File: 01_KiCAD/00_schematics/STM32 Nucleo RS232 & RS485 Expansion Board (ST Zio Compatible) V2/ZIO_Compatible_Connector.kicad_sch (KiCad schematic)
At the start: 8 parts, among them CN1 Conn_02x10_Odd_Even, CN2 Conn_02x08_Odd_Even, CN3 Conn_02x17_Odd_Even, CN4 Conn_02x15_Odd_Even, Q1 BSS84

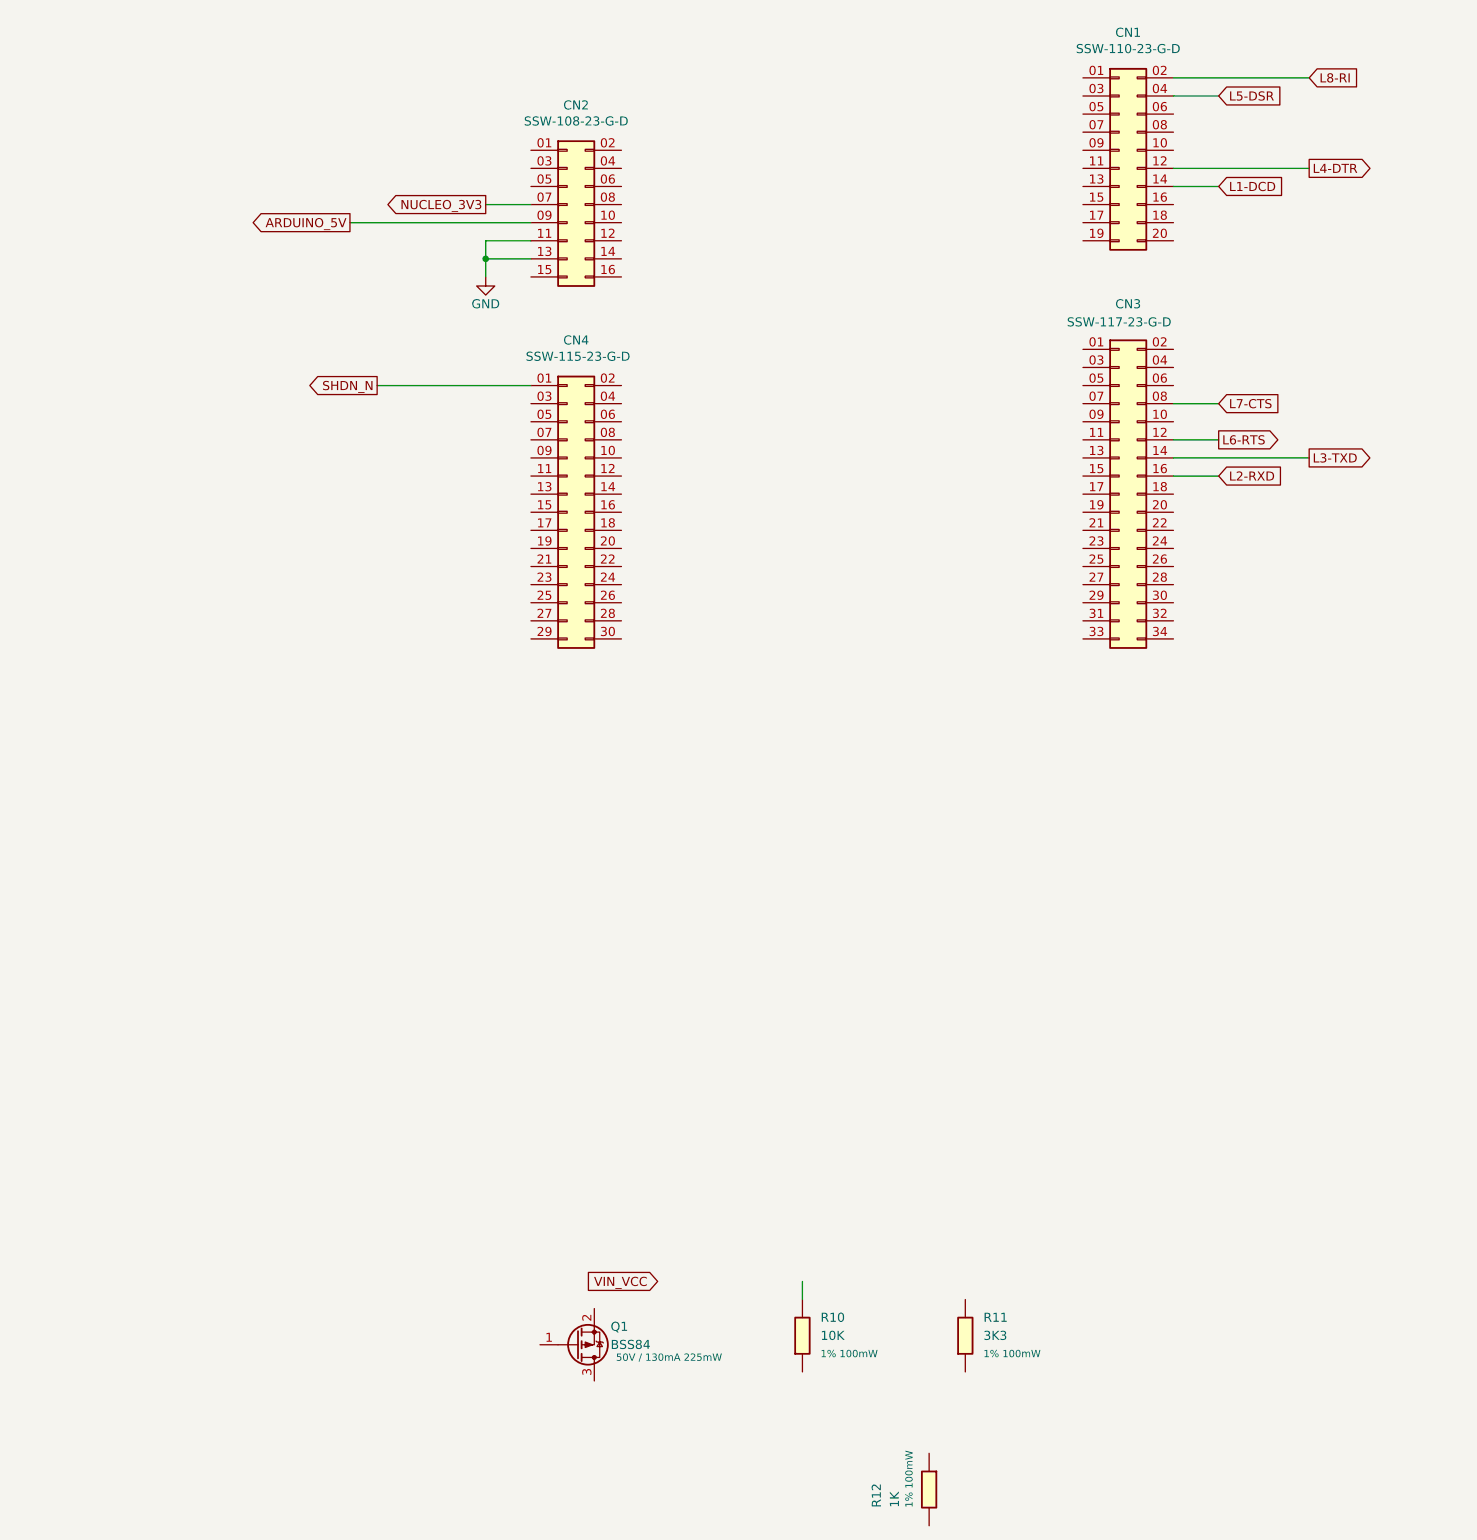
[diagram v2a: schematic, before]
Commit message: Added components and change device
Added dual Schmidt trigger input SN74LVC2G14DBV for LED Rx and Tx control.
Changed sn74hcs245 for alternate part sn74lvc245a for larger footprint and better availability with LCSC.
Difference is sn74lvc245a has no Schmidt-trigger inputs but instead just normal inputs. Fot details see dataseet. Both devices use exact same pin number and configuration except sn74lvc245a has no thermal pad or exposed pad like the sn74hcs245 has.
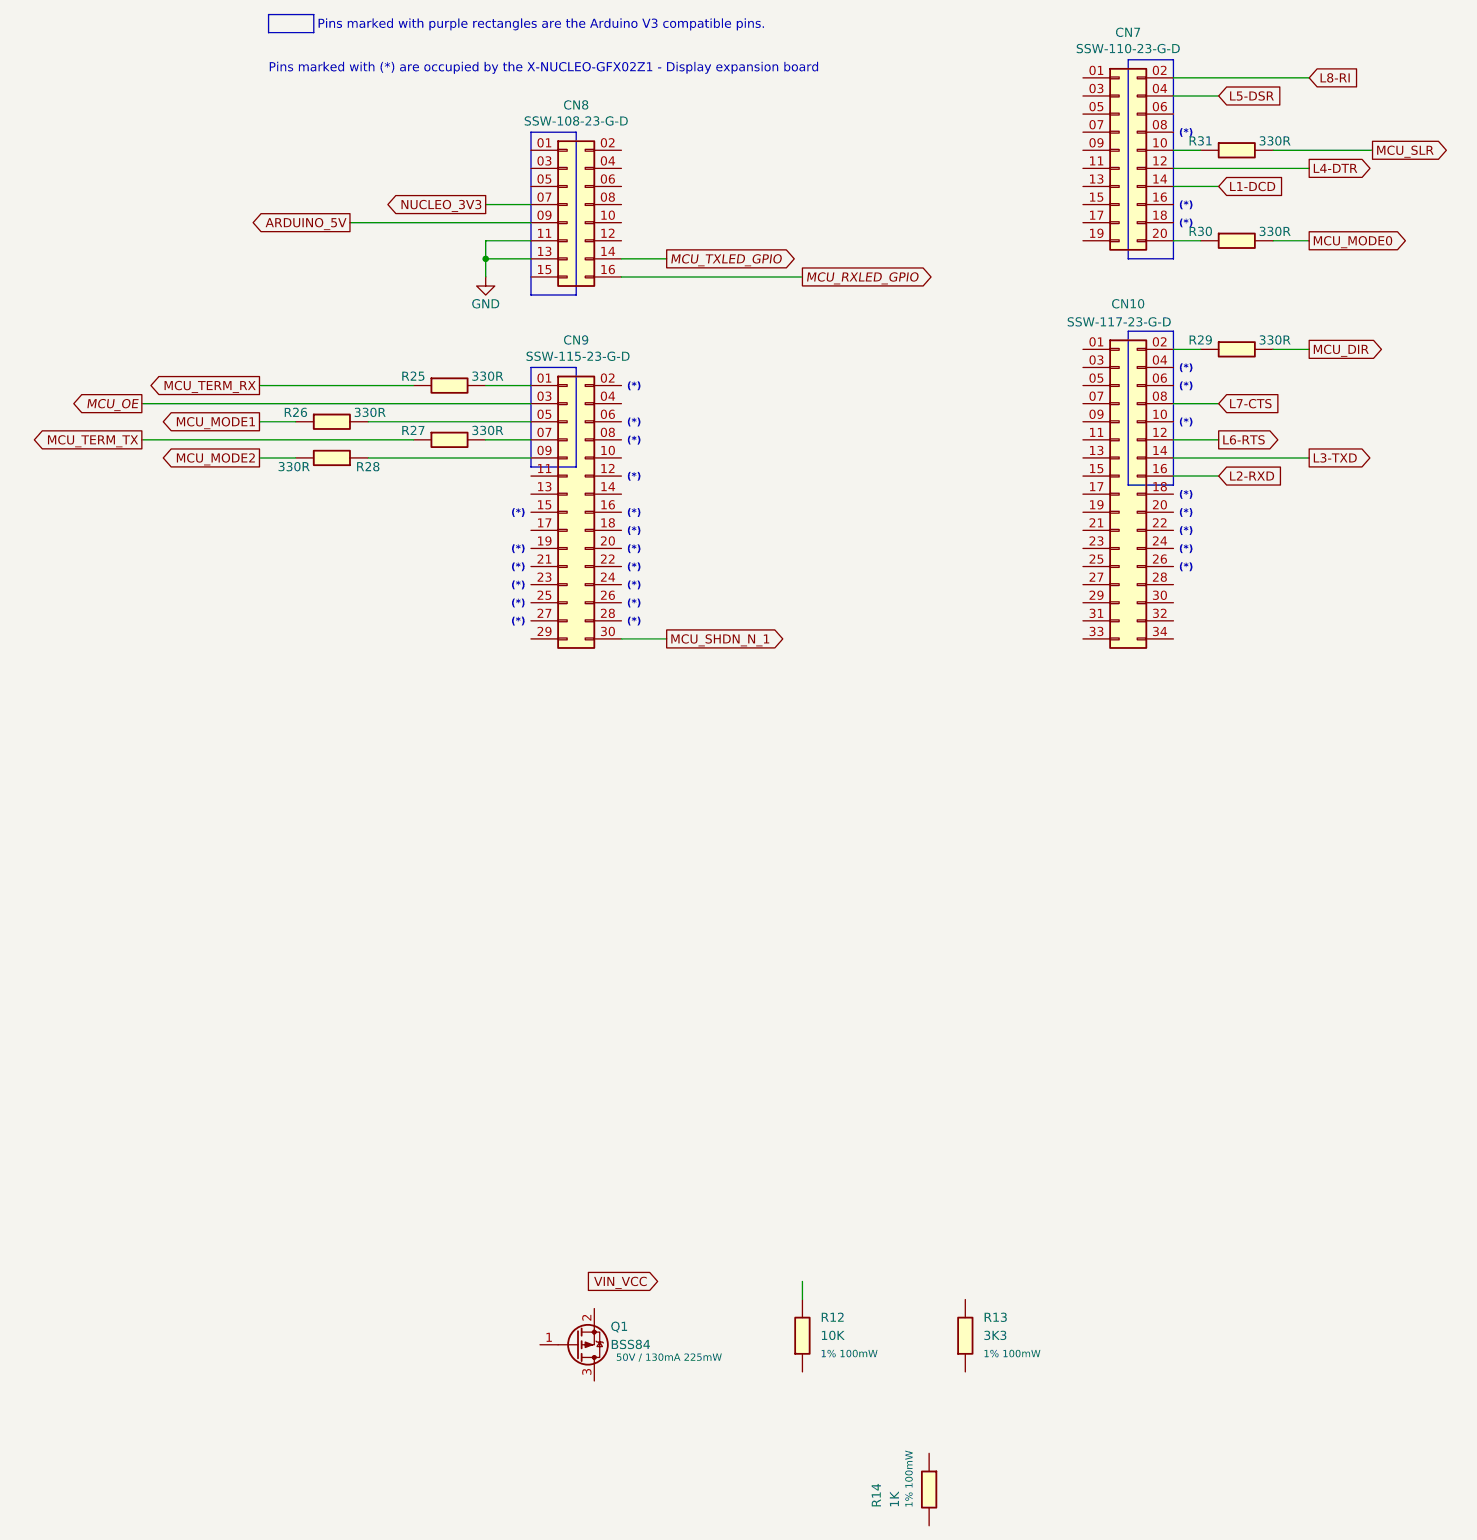
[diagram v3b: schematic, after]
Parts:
- added R25, R26, R27, R28, R29, R30, R31: 330R, PCM_fab:R_0603, symbol PCM_fab:R_0603
- renumbered CN3 to CN10, CN1 to CN7, CN2 to CN8, CN4 to CN9, R10 to R12, R11 to R13, R12 to R14
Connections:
- net MCU_OE: now reaches CN9.03 (Pin_3)
- net at CN9.05 (Pin_5): now also R26.1
- net at CN9.07 (Pin_7): now also R27.1
- net at CN9.09 (Pin_9): now also R28.2
- net MCU_SHDN_N_1: now reaches CN9.30 (Pin_30)
- net at CN7.10 (Pin_10): now also R31.2
- net at CN7.20 (Pin_20): now also R30.2
- net MCU_TXLED_GPIO: now reaches CN8.14 (Pin_14)
- net MCU_RXLED_GPIO: now reaches CN8.16 (Pin_16)
- net at CN10.02 (Pin_2): now also R29.2
- net SHDN_N: no longer names the net of CN9.01 (Pin_1)
- net SHDN_N: now also R25.1
- new net MCU_DIR: R29.1
- new net MCU_MODE0: R30.1
- new net MCU_MODE1: R26.2
- new net MCU_MODE2: R28.1
- new net MCU_SLR: R31.1
- new net MCU_TERM_RX: R25.2
- new net MCU_TERM_TX: R27.2
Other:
- note added: "(*)"
- note added: "Pins marked with (*) are occupied by the X-NUCLEO-GFX02Z1 - Display expansion board"
- note added: "Pins marked with purple rectangles are the Arduino V3 compatible pins."

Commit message: Finisching touches to schematics
Finalizing the schematics and double-check all connections throughout the different sheets.
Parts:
- renumbered Q1 to Q2, R31 to R34, R30 to R35, R29 to R36, R25 to R37, R26 to R38, R27 to R39, R28 to R40, R12 to R41, R13 to R42, R14 to R43
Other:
- note added: "(VREF)"
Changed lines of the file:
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@@
 		)
 	)
+	(text "(VREF)"
+		(exclude_from_sim no)
+		(at 192.278 59.944 0)
+		(effects
+			(font
+				(size 1.016 1.016)
+				(thickness 0.2032)
+				(bold yes)
+			)
+		)
+	)
 	(text "(*)"
 		(exclude_from_sim no)
@@
 		(on_board yes)
 		(dnp no)
-		(property "Reference" "R25"
+		(property "Reference" "R37"
 			(at 82.55 96.52 90)
 			(effects
@@
 			(project "STM32 Nucleo RS232 & RS485 Expansion Board (ST Zio Compatible) V2"
 				(path "/080f83b7-8913-48e8-ab8e-79cb12295542/067a36dd-1222-49fa-b4c7-0b289d0be8ff"
-					(reference "R25")
+					(reference "R37")
 					(unit 1)
 				)
@@
 		(on_board yes)
 		(dnp no)
-		(property "Reference" "R26"
+		(property "Reference" "R38"
 			(at 66.04 101.6 90)
 			(effects
@@
 			(project "STM32 Nucleo RS232 & RS485 Expansion Board (ST Zio Compatible) V2"
 				(path "/080f83b7-8913-48e8-ab8e-79cb12295542/067a36dd-1222-49fa-b4c7-0b289d0be8ff"
-					(reference "R26")
+					(reference "R38")
 					(unit 1)
 				)
@@
 		(on_board yes)
 		(dnp no)
-		(property "Reference" "R14"
+		(property "Reference" "R43"
 			(at 147.574 255.27 90)
 			(effects
@@
 			(project "STM32 Nucleo RS232 & RS485 Expansion Board (ST Zio Compatible) V2"
 				(path "/080f83b7-8913-48e8-ab8e-79cb12295542/067a36dd-1222-49fa-b4c7-0b289d0be8ff"
-					(reference "R14")
+					(reference "R43")
 					(unit 1)
 				)
@@
 		(on_board yes)
 		(dnp no)
-		(property "Reference" "Q1"
+		(property "Reference" "Q2"
 			(at 110.236 229.87 0)
 			(effects
@@
 			(project "STM32 Nucleo RS232 & RS485 Expansion Board (ST Zio Compatible) V2"
 				(path "/080f83b7-8913-48e8-ab8e-79cb12295542/067a36dd-1222-49fa-b4c7-0b289d0be8ff"
-					(reference "Q1")
+					(reference "Q2")
 					(unit 1)
 				)
@@
 		(on_board yes)
 		(dnp no)
-		(property "Reference" "R30"
+		(property "Reference" "R35"
 			(at 193.04 76.2 90)
 			(effects
@@
 			(project "STM32 Nucleo RS232 & RS485 Expansion Board (ST Zio Compatible) V2"
 				(path "/080f83b7-8913-48e8-ab8e-79cb12295542/067a36dd-1222-49fa-b4c7-0b289d0be8ff"
-					(reference "R30")
+					(reference "R35")
 					(unit 1)
 				)
@@
 		(on_board yes)
 		(dnp no)
-		(property "Reference" "R27"
+		(property "Reference" "R39"
 			(at 82.55 104.14 90)
 			(effects
@@
 			(project "STM32 Nucleo RS232 & RS485 Expansion Board (ST Zio Compatible) V2"
 				(path "/080f83b7-8913-48e8-ab8e-79cb12295542/067a36dd-1222-49fa-b4c7-0b289d0be8ff"
-					(reference "R27")
+					(reference "R39")
 					(unit 1)
 				)
@@
 		(on_board yes)
 		(dnp no)
-		(property "Reference" "R28"
+		(property "Reference" "R40"
 			(at 76.2 109.22 90)
 			(effects
@@
 			(project "STM32 Nucleo RS232 & RS485 Expansion Board (ST Zio Compatible) V2"
 				(path "/080f83b7-8913-48e8-ab8e-79cb12295542/067a36dd-1222-49fa-b4c7-0b289d0be8ff"
-					(reference "R28")
+					(reference "R40")
 					(unit 1)
 				)
@@
 		(on_board yes)
 		(dnp no)
-		(property "Reference" "R31"
+		(property "Reference" "R34"
 			(at 193.04 63.5 90)
 			(effects
@@
 			(project "STM32 Nucleo RS232 & RS485 Expansion Board (ST Zio Compatible) V2"
 				(path "/080f83b7-8913-48e8-ab8e-79cb12295542/067a36dd-1222-49fa-b4c7-0b289d0be8ff"
-					(reference "R31")
+					(reference "R34")
 					(unit 1)
 				)
@@
 		(dnp no)
 		(fields_autoplaced yes)
-		(property "Reference" "R12"
+		(property "Reference" "R41"
 			(at 139.7 228.5999 0)
 			(effects
@@
 			(project "STM32 Nucleo RS232 & RS485 Expansion Board (ST Zio Compatible) V2"
 				(path "/080f83b7-8913-48e8-ab8e-79cb12295542/067a36dd-1222-49fa-b4c7-0b289d0be8ff"
-					(reference "R12")
+					(reference "R41")
 					(unit 1)
 				)
@@
 		(dnp no)
 		(fields_autoplaced yes)
-		(property "Reference" "#PWR030"
+		(property "Reference" "#PWR047"
 			(at 92.71 88.9 0)
 			(effects
@@
 			(project ""
 				(path "/080f83b7-8913-48e8-ab8e-79cb12295542/067a36dd-1222-49fa-b4c7-0b289d0be8ff"
-					(reference "#PWR030")
+					(reference "#PWR047")
 					(unit 1)
 				)
@@
 		(on_board yes)
 		(dnp no)
-		(property "Reference" "R29"
+		(property "Reference" "R36"
 			(at 193.04 91.44 90)
 			(effects
@@
 			(project "STM32 Nucleo RS232 & RS485 Expansion Board (ST Zio Compatible) V2"
 				(path "/080f83b7-8913-48e8-ab8e-79cb12295542/067a36dd-1222-49fa-b4c7-0b289d0be8ff"
-					(reference "R29")
+					(reference "R36")
 					(unit 1)
 				)
@@
 		(dnp no)
 		(fields_autoplaced yes)
-		(property "Reference" "R13"
+		(property "Reference" "R42"
 			(at 162.56 228.5999 0)
 			(effects
@@
 			(project "STM32 Nucleo RS232 & RS485 Expansion Board (ST Zio Compatible) V2"
 				(path "/080f83b7-8913-48e8-ab8e-79cb12295542/067a36dd-1222-49fa-b4c7-0b289d0be8ff"
-					(reference "R13")
+					(reference "R42")
 					(unit 1)
 				)
